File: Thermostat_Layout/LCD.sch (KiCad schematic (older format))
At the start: 3 parts, among them J3 LCD_HEADER

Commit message: Update schematic
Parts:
- renumbered J3 to J5, R7 to R11
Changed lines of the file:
@@
 $EndDescr
 $Comp
-L SparkFun-Connectors:CONN_16 J3
+L SparkFun-Connectors:CONN_16 J5
 U 1 1 5D426017
 P 4900 4250
-F 0 "J3" H 4833 6060 45  0000 C CNN
+F 0 "J5" H 4833 6060 45  0000 C CNN
 F 1 "LCD_HEADER" H 4833 5976 45  0000 C CNN
 F 2 "Connector_PinHeader_2.54mm:PinHeader_1x16_P2.54mm_Vertical" H 4900 5950 20  0001 C CNN
@@
 $EndComp
 $Comp
-L SparkFun-PowerSymbols:GND #GND0110
+L SparkFun-PowerSymbols:GND #GND016
 U 1 1 5D429987
 P 5100 4250
-F 0 "#GND0110" H 5150 4200 45  0001 L BNN
+F 0 "#GND016" H 5150 4200 45  0001 L BNN
 F 1 "GND" H 5100 4080 45  0000 C CNN
 F 2 "" H 5100 4150 60  0001 C CNN
@@
 LCD_LED
 $Comp
-L Device:R_US R7
+L Device:R_US R11
 U 1 1 5D42C1C9
 P 6250 3000
-F 0 "R7" H 6318 3046 50  0000 L CNN
+F 0 "R11" H 6318 3046 50  0000 L CNN
 F 1 "220" H 6318 2955 50  0000 L CNN
 F 2 "Resistors:0402" V 6290 2990 50  0001 C CNN
@@
 	6250 4150 6250 3150
 $Comp
-L SparkFun-PowerSymbols:3.3V #SUPPLY0107
+L SparkFun-PowerSymbols:3.3V #SUPPLY09
 U 1 1 5D42E053
 P 6450 4150
-F 0 "#SUPPLY0107" H 6500 4150 45  0001 L BNN
+F 0 "#SUPPLY09" H 6500 4150 45  0001 L BNN
 F 1 "3.3V" H 6450 4426 45  0000 C CNN
 F 2 "XXX-00000" H 6450 4331 60  0000 C CNN
@@
 	8050 3200 8400 3200
 $Comp
-L SparkFun-PowerSymbols:3.3V #SUPPLY0108
+L SparkFun-PowerSymbols:3.3V #SUPPLY010
 U 1 1 5D4305D6
 P 7900 2800
-F 0 "#SUPPLY0108" H 7950 2800 45  0001 L BNN
+F 0 "#SUPPLY010" H 7950 2800 45  0001 L BNN
 F 1 "3.3V" H 7900 3076 45  0000 C CNN
 F 2 "XXX-00000" H 7900 2981 60  0000 C CNN
@@
 $EndComp
 $Comp
-L SparkFun-PowerSymbols:GND #GND0111
+L SparkFun-PowerSymbols:GND #GND017
 U 1 1 5D430FB1
 P 7900 3650
-F 0 "#GND0111" H 7950 3600 45  0001 L BNN
+F 0 "#GND017" H 7950 3600 45  0001 L BNN
 F 1 "GND" H 7900 3480 45  0000 C CNN
 F 2 "" H 7900 3550 60  0001 C CNN

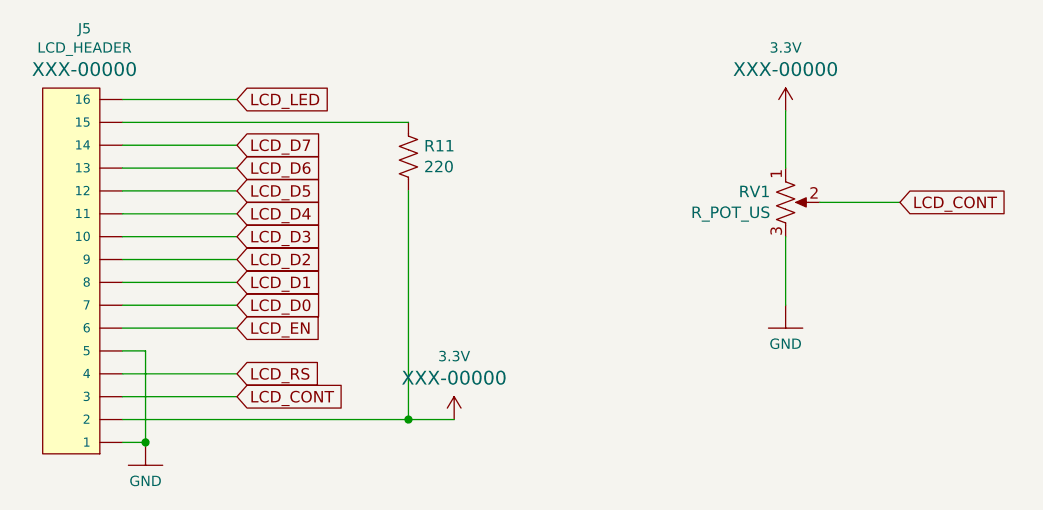
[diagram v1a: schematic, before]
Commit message: FInalize schematic for thermostat
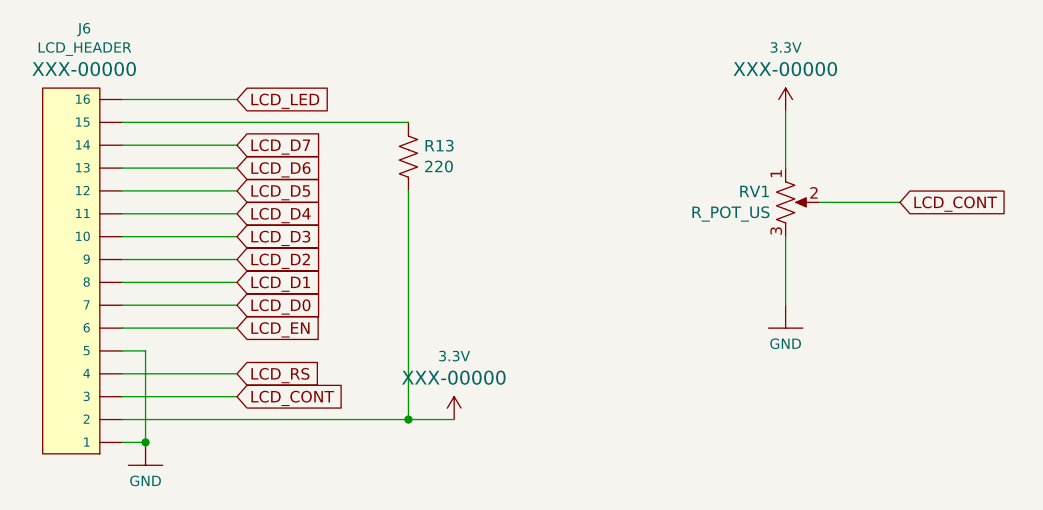
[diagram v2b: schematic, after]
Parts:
- renumbered J5 to J6, R11 to R13
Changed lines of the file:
@@
 $EndDescr
 $Comp
-L SparkFun-Connectors:CONN_16 J5
+L SparkFun-Connectors:CONN_16 J6
 U 1 1 5D426017
 P 4900 4250
-F 0 "J5" H 4833 6060 45  0000 C CNN
+F 0 "J6" H 4833 6060 45  0000 C CNN
 F 1 "LCD_HEADER" H 4833 5976 45  0000 C CNN
 F 2 "Connector_PinHeader_2.54mm:PinHeader_1x16_P2.54mm_Vertical" H 4900 5950 20  0001 C CNN
@@
 $EndComp
 $Comp
-L SparkFun-PowerSymbols:GND #GND016
+L SparkFun-PowerSymbols:GND #GND014
 U 1 1 5D429987
 P 5100 4250
-F 0 "#GND016" H 5150 4200 45  0001 L BNN
+F 0 "#GND014" H 5150 4200 45  0001 L BNN
 F 1 "GND" H 5100 4080 45  0000 C CNN
 F 2 "" H 5100 4150 60  0001 C CNN
@@
 LCD_LED
 $Comp
-L Device:R_US R11
+L Device:R_US R13
 U 1 1 5D42C1C9
 P 6250 3000
-F 0 "R11" H 6318 3046 50  0000 L CNN
+F 0 "R13" H 6318 3046 50  0000 L CNN
 F 1 "220" H 6318 2955 50  0000 L CNN
 F 2 "Resistors:0402" V 6290 2990 50  0001 C CNN
@@
 	6250 4150 6250 3150
 $Comp
-L SparkFun-PowerSymbols:3.3V #SUPPLY09
+L SparkFun-PowerSymbols:3.3V #SUPPLY08
 U 1 1 5D42E053
 P 6450 4150
-F 0 "#SUPPLY09" H 6500 4150 45  0001 L BNN
+F 0 "#SUPPLY08" H 6500 4150 45  0001 L BNN
 F 1 "3.3V" H 6450 4426 45  0000 C CNN
 F 2 "XXX-00000" H 6450 4331 60  0000 C CNN
@@
 	8050 3200 8400 3200
 $Comp
-L SparkFun-PowerSymbols:3.3V #SUPPLY010
+L SparkFun-PowerSymbols:3.3V #SUPPLY09
 U 1 1 5D4305D6
 P 7900 2800
-F 0 "#SUPPLY010" H 7950 2800 45  0001 L BNN
+F 0 "#SUPPLY09" H 7950 2800 45  0001 L BNN
 F 1 "3.3V" H 7900 3076 45  0000 C CNN
 F 2 "XXX-00000" H 7900 2981 60  0000 C CNN
@@
 $EndComp
 $Comp
-L SparkFun-PowerSymbols:GND #GND017
+L SparkFun-PowerSymbols:GND #GND015
 U 1 1 5D430FB1
 P 7900 3650
-F 0 "#GND017" H 7950 3600 45  0001 L BNN
+F 0 "#GND015" H 7950 3600 45  0001 L BNN
 F 1 "GND" H 7900 3480 45  0000 C CNN
 F 2 "" H 7900 3550 60  0001 C CNN

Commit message: Schematic and PCB layout for thermostat
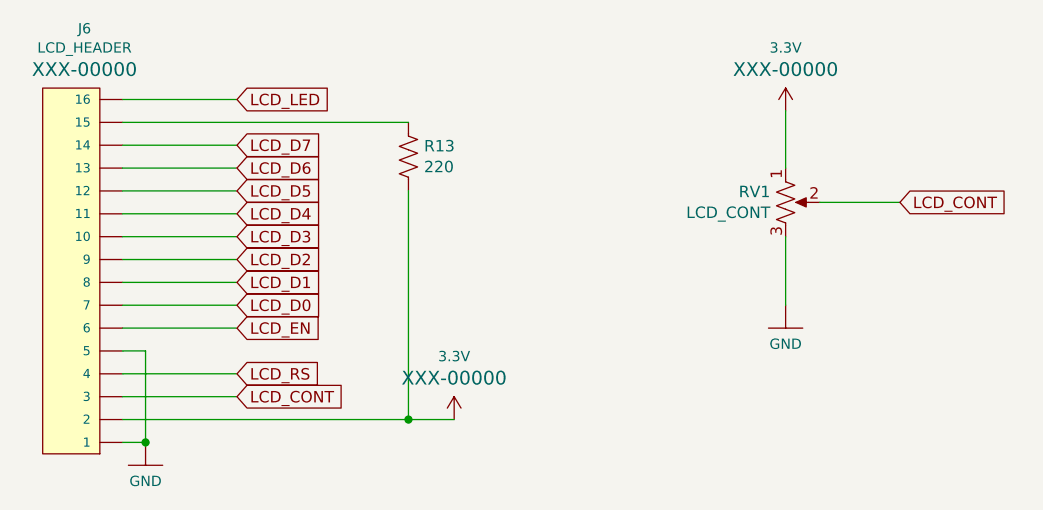
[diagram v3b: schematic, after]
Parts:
- RV1: value R_POT_US -> LCD_CONT
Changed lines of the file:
@@
 P 7900 3200
 F 0 "RV1" H 7833 3246 50  0000 R CNN
-F 1 "R_POT_US" H 7833 3155 50  0000 R CNN
+F 1 "LCD_CONT" H 7833 3155 50  0000 R CNN
 F 2 "Potentiometer_SMD:Potentiometer_Bourns_TC33X_Vertical" H 7900 3200 50  0001 C CNN
 F 3 "~" H 7900 3200 50  0001 C CNN

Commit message: Move some components around
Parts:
- J6: footprint Connector_PinHeader_2.54mm:PinHeader_1x16_P2.54mm_Vertical -> Connector_JST:JST_PH_B16B-PH-K_1x16_P2.00mm_Vertical
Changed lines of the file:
@@
 F 0 "J6" H 4833 6060 45  0000 C CNN
 F 1 "LCD_HEADER" H 4833 5976 45  0000 C CNN
-F 2 "Connector_PinHeader_2.54mm:PinHeader_1x16_P2.54mm_Vertical" H 4900 5950 20  0001 C CNN
+F 2 "Connector_JST:JST_PH_B16B-PH-K_1x16_P2.00mm_Vertical" H 4900 5950 20  0001 C CNN
 F 3 "" H 4900 4250 50  0001 C CNN
 F 4 "XXX-00000" H 4833 5881 60  0000 C CNN "Field4"
